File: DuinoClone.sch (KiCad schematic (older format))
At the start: 13 parts, among them U1 DS1337S+, U2 24LC1025, U3 24LC1025, U4 ATMEGA328P-AU, Y1 Crystal 32MHz, Y2 Crystal 16MHz

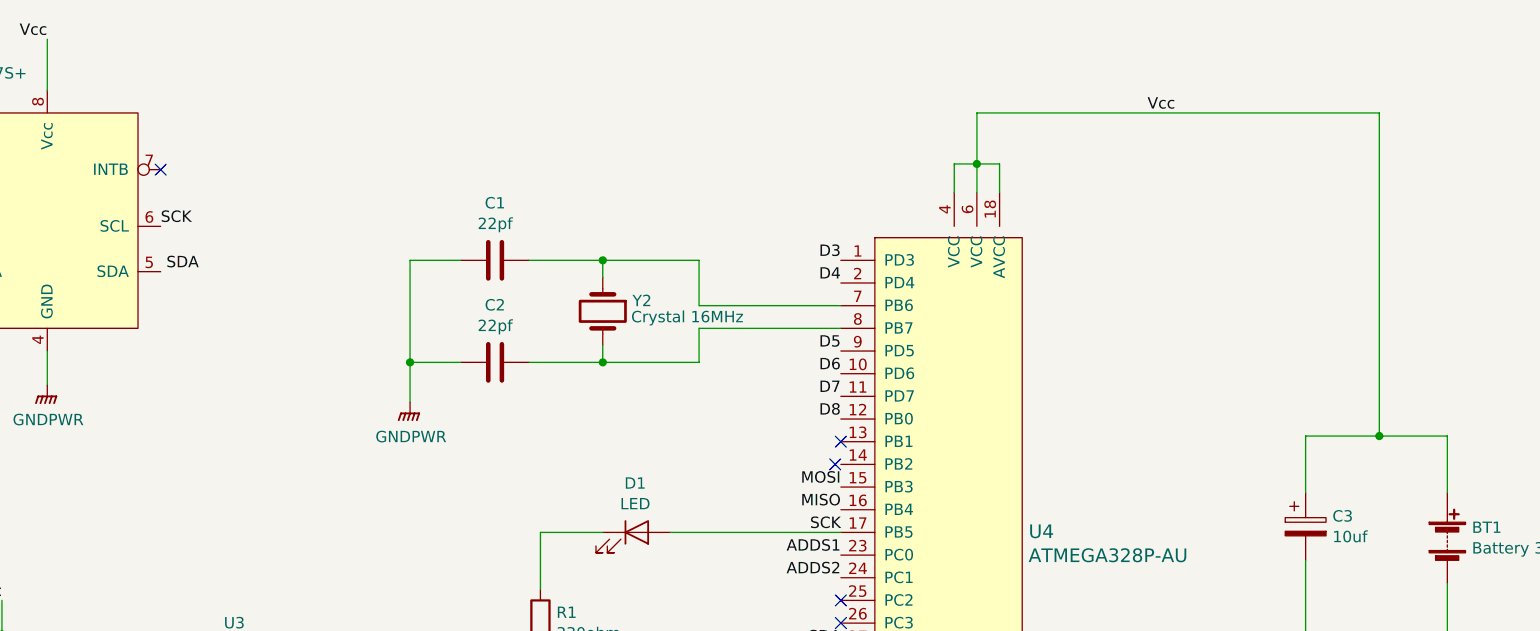
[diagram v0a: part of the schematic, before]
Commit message: Added power flag symbol
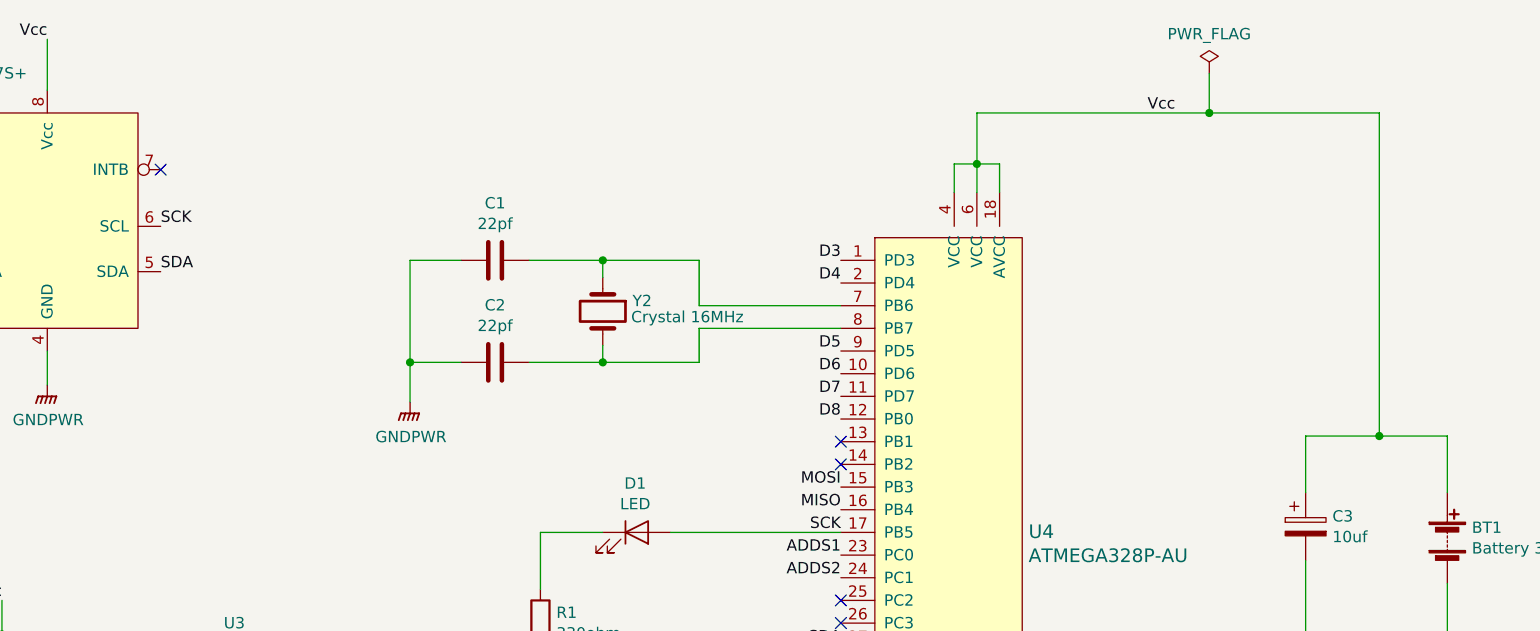
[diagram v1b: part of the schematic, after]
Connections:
- net SDA: now also U1.5 (SDA)
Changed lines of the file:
@@
 	6425 5250 6525 5250
 $Comp
-L power:GNDPWR #PWR?
+L power:GNDPWR #PWR0101
 U 1 1 5CE88593
 P 4250 7250
-F 0 "#PWR?" H 4250 7050 50  0001 C CNN
+F 0 "#PWR0101" H 4250 7050 50  0001 C CNN
 F 1 "GNDPWR" H 4254 7096 50  0000 C CNN
 F 2 "" H 4250 7200 50  0001 C CNN
@@
 	975  2275 975  2150
 $Comp
-L power:GNDPWR #PWR?
+L power:GNDPWR #PWR0102
 U 1 1 5CEA075E
 P 2325 2825
-F 0 "#PWR?" H 2325 2625 50  0001 C CNN
+F 0 "#PWR0102" H 2325 2625 50  0001 C CNN
 F 1 "GNDPWR" H 2329 2671 50  0000 C CNN
 F 2 "" H 2325 2775 50  0001 C CNN
@@
 Text Label 2825 2125 0    50   ~ 0
 SCK
-Text Label 2850 2325 0    50   ~ 0
+Text Label 2825 2325 0    50   ~ 0
 SDA
 Text Label 2125 3775 2    50   ~ 0
@@
 	2125 3925 1525 3925
 $Comp
-L power:GNDPWR #PWR?
+L power:GNDPWR #PWR0103
 U 1 1 5CEA966C
 P 2125 4850
-F 0 "#PWR?" H 2125 4650 50  0001 C CNN
+F 0 "#PWR0103" H 2125 4650 50  0001 C CNN
 F 1 "GNDPWR" H 2129 4696 50  0000 C CNN
 F 2 "" H 2125 4800 50  0001 C CNN
@@
 ADDS2
 $Comp
-L power:GNDPWR #PWR?
+L power:GNDPWR #PWR0104
 U 1 1 5CEB7742
 P 8200 4125
-F 0 "#PWR?" H 8200 3925 50  0001 C CNN
+F 0 "#PWR0104" H 8200 3925 50  0001 C CNN
 F 1 "GNDPWR" H 8204 3971 50  0000 C CNN
 F 2 "" H 8200 4075 50  0001 C CNN
@@
 	6425 1850 6425 1625
 Wire Wire Line
-	6425 1625 8200 1625
+	6425 1625 7450 1625
 Wire Wire Line
 	8200 1625 8200 3050
@@
 	4775 2725 4775 2650
 $Comp
-L power:GNDPWR #PWR?
+L power:GNDPWR #PWR0105
 U 1 1 5CED4674
 P 3925 2900
-F 0 "#PWR?" H 3925 2700 50  0001 C CNN
+F 0 "#PWR0105" H 3925 2700 50  0001 C CNN
 F 1 "GNDPWR" H 3929 2746 50  0000 C CNN
 F 2 "" H 3925 2850 50  0001 C CNN
@@
 	4500 3475 4500 3725
 $Comp
-L power:GNDPWR #PWR?
+L power:GNDPWR #PWR0106
 U 1 1 5CEF2AB9
 P 4500 4125
-F 0 "#PWR?" H 4500 3925 50  0001 C CNN
+F 0 "#PWR0106" H 4500 3925 50  0001 C CNN
 F 1 "GNDPWR" H 4504 3971 50  0000 C CNN
 F 2 "" H 4500 4075 50  0001 C CNN
@@
 	5050 4925 4900 4925
 $Comp
-L power:GNDPWR #PWR?
+L power:GNDPWR #PWR0107
 U 1 1 5CF0AC6C
 P 6425 5400
-F 0 "#PWR?" H 6425 5200 50  0001 C CNN
+F 0 "#PWR0107" H 6425 5200 50  0001 C CNN
 F 1 "GNDPWR" H 6429 5246 50  0000 C CNN
 F 2 "" H 6425 5350 50  0001 C CNN
@@
 	6425 5400 6425 5250
 NoConn ~ 5825 3075
-NoConn ~ 5800 3175
 NoConn ~ 5825 3775
 NoConn ~ 5825 3875
@@
 NoConn ~ 5825 4575
 NoConn ~ 5825 4775
+$Comp
+L power:PWR_FLAG #FLG0101
+U 1 1 5CF1DF0F
+P 7450 1450
+F 0 "#FLG0101" H 7450 1525 50  0001 C CNN
+F 1 "PWR_FLAG" H 7450 1623 50  0000 C CNN
+F 2 "" H 7450 1450 50  0001 C CNN
+F 3 "~" H 7450 1450 50  0001 C CNN
+	1    7450 1450
+	1    0    0    -1
+$EndComp
+Wire Wire Line
+	7450 1450 7450 1625
+Connection ~ 7450 1625
+Wire Wire Line
+	7450 1625 8200 1625
+NoConn ~ 5825 3175
 $EndSCHEMATC

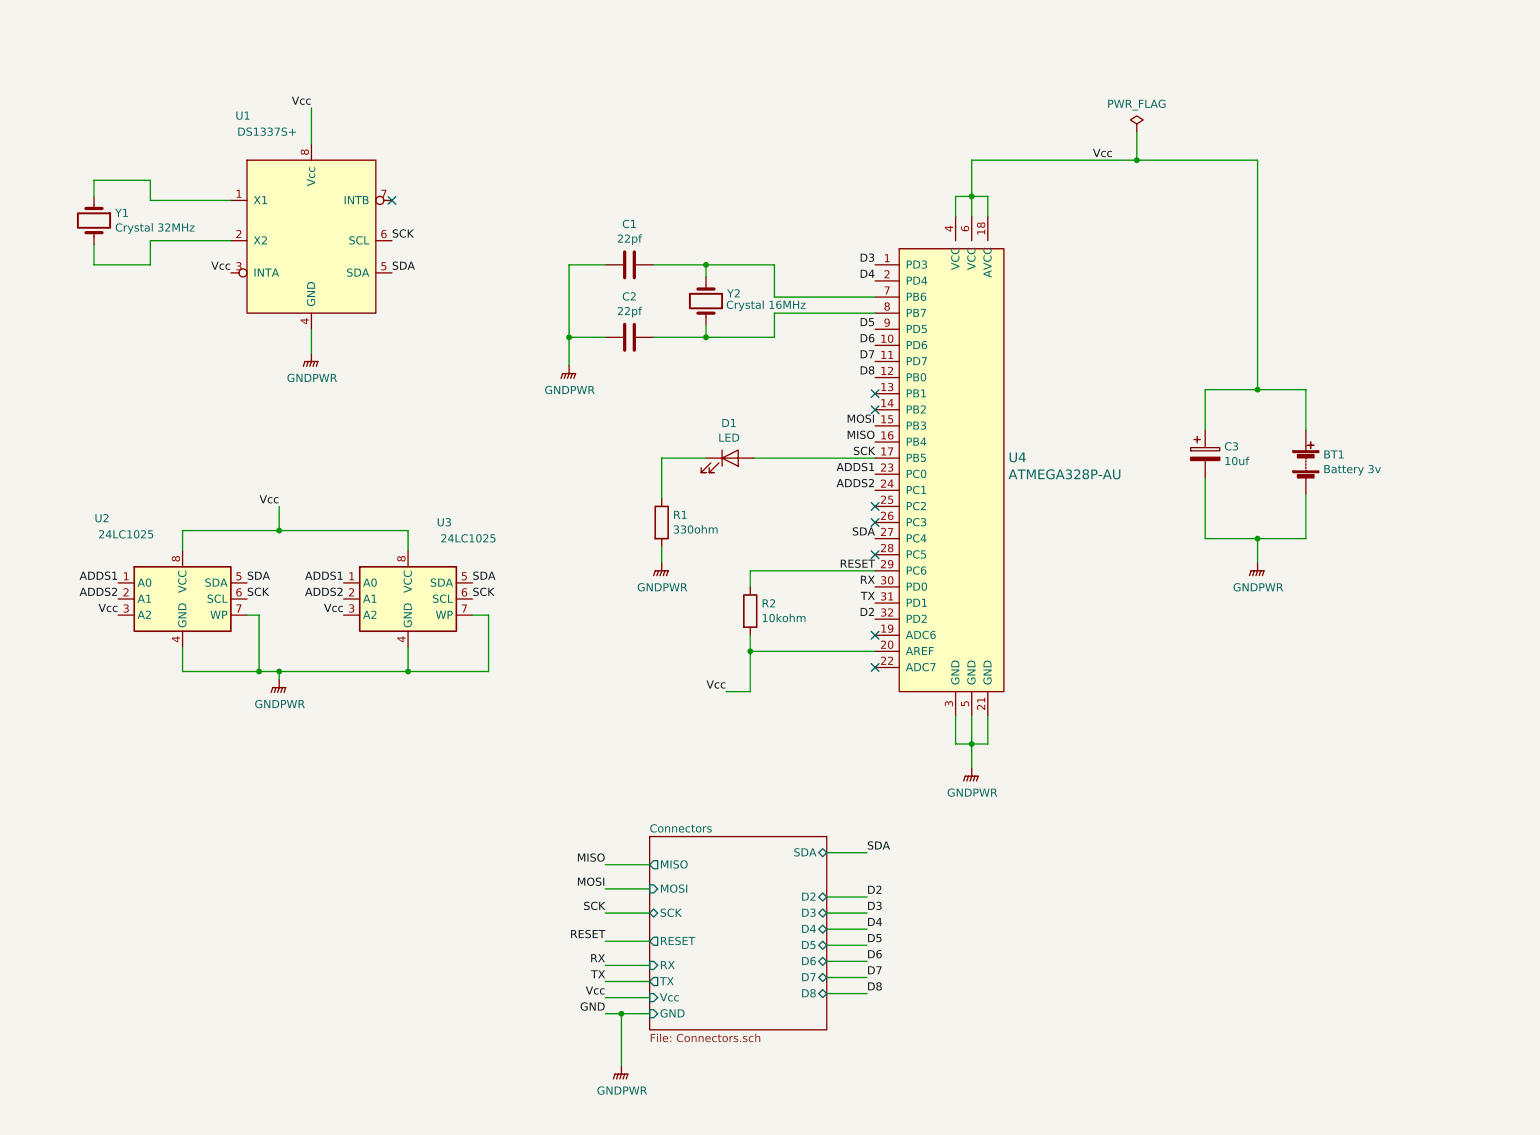
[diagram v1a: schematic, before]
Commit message: Added functional block descriptions
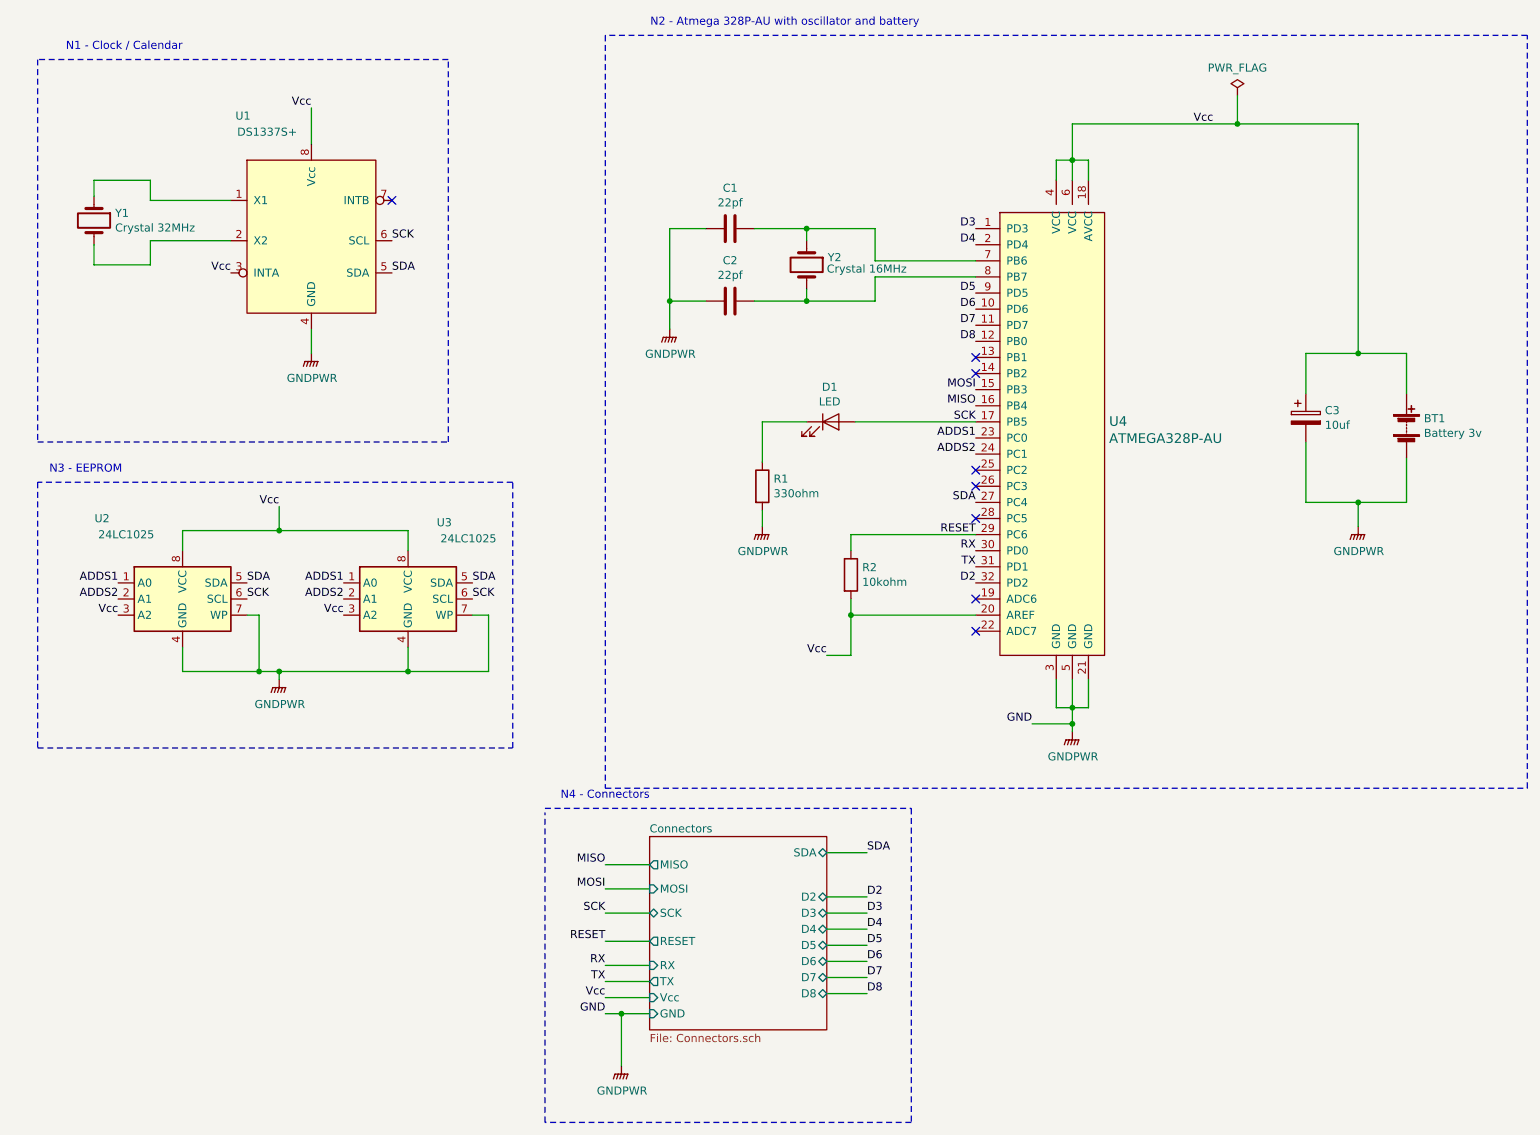
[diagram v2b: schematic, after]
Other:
- note added: "N1 - Clock / Calendar\n"
- note added: "N2 - Atmega 328P-AU with oscillator and battery"
- note added: "N3 - EEPROM"
- note added: "N4 - Connectors"
- moved on the sheet: BT1, C1, C2, C3, D1, R1, R2, U4, Y2
